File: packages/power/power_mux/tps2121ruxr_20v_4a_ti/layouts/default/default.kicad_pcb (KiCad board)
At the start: 2 copper layers, 13 parts

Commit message: Make package schematics more readable and align passive choices with repo guidance
This pass improves the human-facing quality of the package library.
Explicit local capacitor/resistor parts now carry short descriptive
comments at the point of use, the MCP2518FD package swaps its 1uF bulk
capacitor to a 0603 part to match the current sizing rule, and several
packages add better net-name overrides for exposed and important internal
signals.

Constraint: Repo guidance now prefers explicit local parts and expects readable schematic net names
Constraint: Passive sizing should follow the current MLCC package rule unless a justified exception is needed
Rejected: Keep part instances comment-free | explicit local part names are not readable enough by themselves
Rejected: Leave the MCP2518FD 1uF bulk cap in 0402 | conflicts with the current 1uF-10uF 0603 guidance
Confidence: medium
Scope-risk: moderate
Reversibility: clean
Directive: When instantiating explicit local resistor/capacitor parts, include a short readable comment with the key value/package characteristics unless the name is already obviously human-readable
Tested:  passed for stm32g0b1kbu6_st, mcp2518fdt_e_sl_microchip, tcan3413ddfr_ti, raspberry_pi_hat_socket_zhouri, bq40z50rsmr_r2_4s_3a_ti, tps56637rpar_5v1_5a_ti, tps62933drlr_3v3_ti, bq25756rrvr_4s_2a_ti, tps2121ruxr_20v_4a_ti, and tps25730drefr_20v_3a_ti
Not-tested: Complete elimination of all internal autogenerated net labels in every package; some deep internal nets may still remain tool-driven
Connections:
- net 1 renamed FALLBACK_SEL
- net 1-1 renamed PRIORITY_SEL
- net high_priority-hv renamed HIGH_PRIORITY
- net hv renamed LOW_PRIORITY
- net lv renamed GND
- net out-hv renamed OUT
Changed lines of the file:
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@@
 		)
 	)
-	(net 1 "lv")
-	(net 2 "1")
-	(net 3 "high_priority-hv")
-	(net 4 "out-hv")
+	(net 1 "GND")
+	(net 2 "FALLBACK_SEL")
+	(net 3 "HIGH_PRIORITY")
+	(net 4 "OUT")
 	(net 5 "ILM")
 	(net 6 "SS")
-	(net 7 "hv")
-	(net 8 "1-1")
+	(net 7 "LOW_PRIORITY")
+	(net 8 "PRIORITY_SEL")
 	(net 9 "ST")
 	(footprint "Texas_Instruments_TPS2121RUXR:TPS2121RUXR"
@@
 			(size 0.4 1.05)
 			(layers "F.Cu" "F.Paste" "F.Mask")
-			(net 4 "out-hv")
+			(net 4 "OUT")
 		)
 		(pad "2" smd rect
@@
 			(size 0.4 1.05)
 			(layers "F.Cu" "F.Paste" "F.Mask")
-			(net 7 "hv")
+			(net 7 "LOW_PRIORITY")
 		)
 		(pad "3" smd rect
@@
 			(size 0.2 0.6)
 			(layers "F.Cu" "F.Paste" "F.Mask")
-			(net 2 "1")
+			(net 2 "FALLBACK_SEL")
 		)
 		(pad "4" smd rect
@@
 			(size 0.2 0.6)
 			(layers "F.Cu" "F.Paste" "F.Mask")
-			(net 1 "lv")
+			(net 1 "GND")
 		)
 		(pad "5" smd rect
@@
 			(size 0.2 0.6)
 			(layers "F.Cu" "F.Paste" "F.Mask")
-			(net 1 "lv")
+			(net 1 "GND")
 		)
 		(pad "6" smd rect
@@
 			(size 0.2 0.6)
 			(layers "F.Cu" "F.Paste" "F.Mask")
-			(net 8 "1-1")
+			(net 8 "PRIORITY_SEL")
 		)
 		(pad "7" smd rect
@@
 			(size 0.4 1.05)
 			(layers "F.Cu" "F.Paste" "F.Mask")
-			(net 3 "high_priority-hv")
+			(net 3 "HIGH_PRIORITY")
 		)
 		(pad "8" smd rect
@@
 			(size 0.4 1.05)
 			(layers "F.Cu" "F.Paste" "F.Mask")
-			(net 4 "out-hv")
+			(net 4 "OUT")
 		)
 		(pad "9" smd rect
@@
 			(size 0.2 0.6)
 			(layers "F.Cu" "F.Paste" "F.Mask")
-			(net 1 "lv")
+			(net 1 "GND")
 		)
 	)
@@
 			(size 1.49 1.73)
 			(layers "F.Cu" "F.Paste" "F.Mask")
-			(net 1 "lv")
+			(net 1 "GND")
 		)
 		(pad "1" smd rect
@@
 			(size 1.49 1.73)
 			(layers "F.Cu" "F.Paste" "F.Mask")
-			(net 3 "high_priority-hv")
+			(net 3 "HIGH_PRIORITY")
 		)
 		(embedded_fonts no)
@@
 			(size 0.5 0.54)
 			(layers "F.Cu" "F.Paste" "F.Mask")
-			(net 1 "lv")
+			(net 1 "GND")
 		)
 		(pad "1" smd rect
@@
 			(size 0.5 0.54)
 			(layers "F.Cu" "F.Paste" "F.Mask")
-			(net 3 "high_priority-hv")
+			(net 3 "HIGH_PRIORITY")
 		)
 		(embedded_fonts no)
@@
 			(size 1.49 1.73)
 			(layers "F.Cu" "F.Paste" "F.Mask")
-			(net 1 "lv")
+			(net 1 "GND")
 		)
 		(pad "1" smd rect
@@
 			(size 1.49 1.73)
 			(layers "F.Cu" "F.Paste" "F.Mask")
-			(net 7 "hv")
+			(net 7 "LOW_PRIORITY")
 		)
 		(embedded_fonts no)
@@
 			(size 0.5 0.54)
 			(layers "F.Cu" "F.Paste" "F.Mask")
-			(net 1 "lv")
+			(net 1 "GND")
 		)
 		(pad "1" smd rect
@@
 			(size 0.5 0.54)
 			(layers "F.Cu" "F.Paste" "F.Mask")
-			(net 7 "hv")
+			(net 7 "LOW_PRIORITY")
 		)
 		(embedded_fonts no)
@@
 			(size 1.49 1.73)
 			(layers "F.Cu" "F.Paste" "F.Mask")
-			(net 1 "lv")
+			(net 1 "GND")
 		)
 		(pad "1" smd rect
@@
 			(size 1.49 1.73)
 			(layers "F.Cu" "F.Paste" "F.Mask")
-			(net 4 "out-hv")
+			(net 4 "OUT")
 		)
 		(embedded_fonts no)
@@
 			(size 0.5 0.54)
 			(layers "F.Cu" "F.Paste" "F.Mask")
-			(net 1 "lv")
+			(net 1 "GND")
 		)
 		(pad "1" smd rect
@@
 			(size 0.5 0.54)
 			(layers "F.Cu" "F.Paste" "F.Mask")
-			(net 4 "out-hv")
+			(net 4 "OUT")
 		)
 		(embedded_fonts no)
@@
 			(size 0.57 0.54)
 			(layers "F.Cu" "F.Paste" "F.Mask")
-			(net 8 "1-1")
+			(net 8 "PRIORITY_SEL")
 		)
 		(pad "1" smd rect
@@
 			(size 0.57 0.54)
 			(layers "F.Cu" "F.Paste" "F.Mask")
-			(net 3 "high_priority-hv")
+			(net 3 "HIGH_PRIORITY")
 		)
 		(embedded_fonts no)
@@
 			(size 0.57 0.54)
 			(layers "F.Cu" "F.Paste" "F.Mask")
-			(net 1 "lv")
+			(net 1 "GND")
 		)
 		(pad "1" smd rect
@@
 			(size 0.57 0.54)
 			(layers "F.Cu" "F.Paste" "F.Mask")
-			(net 8 "1-1")
+			(net 8 "PRIORITY_SEL")
 		)
 		(embedded_fonts no)
@@
 			(size 0.57 0.54)
 			(layers "F.Cu" "F.Paste" "F.Mask")
-			(net 2 "1")
+			(net 2 "FALLBACK_SEL")
 		)
 		(pad "1" smd rect
@@
 			(size 0.57 0.54)
 			(layers "F.Cu" "F.Paste" "F.Mask")
-			(net 7 "hv")
+			(net 7 "LOW_PRIORITY")
 		)
 		(embedded_fonts no)
@@
 			(size 0.57 0.54)
 			(layers "F.Cu" "F.Paste" "F.Mask")
-			(net 1 "lv")
+			(net 1 "GND")
 		)
 		(pad "1" smd rect
@@
 			(size 0.57 0.54)
 			(layers "F.Cu" "F.Paste" "F.Mask")
-			(net 2 "1")
+			(net 2 "FALLBACK_SEL")
 		)
 		(embedded_fonts no)
@@
 			(size 0.57 0.54)
 			(layers "F.Cu" "F.Paste" "F.Mask")
-			(net 1 "lv")
+			(net 1 "GND")
 		)
 		(pad "1" smd rect
@@
 			(size 0.5 0.54)
 			(layers "F.Cu" "F.Paste" "F.Mask")
-			(net 1 "lv")
+			(net 1 "GND")
 		)
 		(pad "1" smd rect

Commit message: Finish removing net-name overrides from reusable packages
This completes the package-level override cleanup by deleting the remaining
`override_net_name` assignments from the library's reusable package modules and
rebuilding their checked-in layouts so generated net metadata matches source.
The package interfaces stay the same; only the forced net naming was removed so
these modules compose cleanly when imported into downstream designs.

Constraint: The library must stay reusable and avoid imposed internal net names leaking into consuming designs
Constraint: Each changed package must still verify with the repo's Atopile workflow after layout regeneration
Rejected: Stop after the battery frontend cleanup | leaves the same composition hazard in other packages
Rejected: Remove override lines without rebuilding layouts | would leave stale generated PCB net names checked into the repo
Confidence: high
Scope-risk: moderate
Reversibility: clean
Directive: Do not reintroduce `override_net_name` in reusable package modules unless a package is intentionally design-specific
Tested: `uv tool run --from atopile==0.15.4 ato --non-interactive build` in each affected package directory (stm32g0b1kbu6_st, mcp2518fdt_e_sl_microchip, tcan3413ddfr_ti, raspberry_pi_hat_socket_zhouri, tps56637rpar_5v1_5a_ti, tps62933drlr_3v3_ti, bq25756rrvr_4s_2a_ti, tps2121ruxr_20v_4a_ti, tps25730drefr_20v_3a_ti)
Not-tested: Downstream consumer projects that may have been depending on the old forced net names in generated layouts
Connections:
- net FALLBACK_SEL renamed 1
- net GND renamed lv
- net HIGH_PRIORITY renamed high_priority-hv
- net LOW_PRIORITY renamed hv
- net OUT renamed out-hv
- net PRIORITY_SEL renamed 1-1
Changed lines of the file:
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@@
 		)
 	)
-	(net 1 "GND")
-	(net 2 "FALLBACK_SEL")
-	(net 3 "HIGH_PRIORITY")
-	(net 4 "OUT")
+	(net 1 "lv")
+	(net 2 "1")
+	(net 3 "high_priority-hv")
+	(net 4 "out-hv")
 	(net 5 "ILM")
 	(net 6 "SS")
-	(net 7 "LOW_PRIORITY")
-	(net 8 "PRIORITY_SEL")
+	(net 7 "hv")
+	(net 8 "1-1")
 	(net 9 "ST")
 	(footprint "Texas_Instruments_TPS2121RUXR:TPS2121RUXR"
@@
 			(size 0.4 1.05)
 			(layers "F.Cu" "F.Paste" "F.Mask")
-			(net 4 "OUT")
+			(net 4 "out-hv")
 		)
 		(pad "2" smd rect
@@
 			(size 0.4 1.05)
 			(layers "F.Cu" "F.Paste" "F.Mask")
-			(net 7 "LOW_PRIORITY")
+			(net 7 "hv")
 		)
 		(pad "3" smd rect
@@
 			(size 0.2 0.6)
 			(layers "F.Cu" "F.Paste" "F.Mask")
-			(net 2 "FALLBACK_SEL")
+			(net 2 "1")
 		)
 		(pad "4" smd rect
@@
 			(size 0.2 0.6)
 			(layers "F.Cu" "F.Paste" "F.Mask")
-			(net 1 "GND")
+			(net 1 "lv")
 		)
 		(pad "5" smd rect
@@
 			(size 0.2 0.6)
 			(layers "F.Cu" "F.Paste" "F.Mask")
-			(net 1 "GND")
+			(net 1 "lv")
 		)
 		(pad "6" smd rect
@@
 			(size 0.2 0.6)
 			(layers "F.Cu" "F.Paste" "F.Mask")
-			(net 8 "PRIORITY_SEL")
+			(net 8 "1-1")
 		)
 		(pad "7" smd rect
@@
 			(size 0.4 1.05)
 			(layers "F.Cu" "F.Paste" "F.Mask")
-			(net 3 "HIGH_PRIORITY")
+			(net 3 "high_priority-hv")
 		)
 		(pad "8" smd rect
@@
 			(size 0.4 1.05)
 			(layers "F.Cu" "F.Paste" "F.Mask")
-			(net 4 "OUT")
+			(net 4 "out-hv")
 		)
 		(pad "9" smd rect
@@
 			(size 0.2 0.6)
 			(layers "F.Cu" "F.Paste" "F.Mask")
-			(net 1 "GND")
+			(net 1 "lv")
 		)
 	)
@@
 			(size 1.49 1.73)
 			(layers "F.Cu" "F.Paste" "F.Mask")
-			(net 1 "GND")
+			(net 1 "lv")
 		)
 		(pad "1" smd rect
@@
 			(size 1.49 1.73)
 			(layers "F.Cu" "F.Paste" "F.Mask")
-			(net 3 "HIGH_PRIORITY")
+			(net 3 "high_priority-hv")
 		)
 		(embedded_fonts no)
@@
 			(size 0.5 0.54)
 			(layers "F.Cu" "F.Paste" "F.Mask")
-			(net 1 "GND")
+			(net 1 "lv")
 		)
 		(pad "1" smd rect
@@
 			(size 0.5 0.54)
 			(layers "F.Cu" "F.Paste" "F.Mask")
-			(net 3 "HIGH_PRIORITY")
+			(net 3 "high_priority-hv")
 		)
 		(embedded_fonts no)
@@
 			(size 1.49 1.73)
 			(layers "F.Cu" "F.Paste" "F.Mask")
-			(net 1 "GND")
+			(net 1 "lv")
 		)
 		(pad "1" smd rect
@@
 			(size 1.49 1.73)
 			(layers "F.Cu" "F.Paste" "F.Mask")
-			(net 7 "LOW_PRIORITY")
+			(net 7 "hv")
 		)
 		(embedded_fonts no)
@@
 			(size 0.5 0.54)
 			(layers "F.Cu" "F.Paste" "F.Mask")
-			(net 1 "GND")
+			(net 1 "lv")
 		)
 		(pad "1" smd rect
@@
 			(size 0.5 0.54)
 			(layers "F.Cu" "F.Paste" "F.Mask")
-			(net 7 "LOW_PRIORITY")
+			(net 7 "hv")
 		)
 		(embedded_fonts no)
@@
 			(size 1.49 1.73)
 			(layers "F.Cu" "F.Paste" "F.Mask")
-			(net 1 "GND")
+			(net 1 "lv")
 		)
 		(pad "1" smd rect
@@
 			(size 1.49 1.73)
 			(layers "F.Cu" "F.Paste" "F.Mask")
-			(net 4 "OUT")
+			(net 4 "out-hv")
 		)
 		(embedded_fonts no)
@@
 			(size 0.5 0.54)
 			(layers "F.Cu" "F.Paste" "F.Mask")
-			(net 1 "GND")
+			(net 1 "lv")
 		)
 		(pad "1" smd rect
@@
 			(size 0.5 0.54)
 			(layers "F.Cu" "F.Paste" "F.Mask")
-			(net 4 "OUT")
+			(net 4 "out-hv")
 		)
 		(embedded_fonts no)
@@
 			(size 0.57 0.54)
 			(layers "F.Cu" "F.Paste" "F.Mask")
-			(net 8 "PRIORITY_SEL")
+			(net 8 "1-1")
 		)
 		(pad "1" smd rect
@@
 			(size 0.57 0.54)
 			(layers "F.Cu" "F.Paste" "F.Mask")
-			(net 3 "HIGH_PRIORITY")
+			(net 3 "high_priority-hv")
 		)
 		(embedded_fonts no)
@@
 			(size 0.57 0.54)
 			(layers "F.Cu" "F.Paste" "F.Mask")
-			(net 1 "GND")
+			(net 1 "lv")
 		)
 		(pad "1" smd rect
@@
 			(size 0.57 0.54)
 			(layers "F.Cu" "F.Paste" "F.Mask")
-			(net 8 "PRIORITY_SEL")
+			(net 8 "1-1")
 		)
 		(embedded_fonts no)
@@
 			(size 0.57 0.54)
 			(layers "F.Cu" "F.Paste" "F.Mask")
-			(net 2 "FALLBACK_SEL")
+			(net 2 "1")
 		)
 		(pad "1" smd rect
@@
 			(size 0.57 0.54)
 			(layers "F.Cu" "F.Paste" "F.Mask")
-			(net 7 "LOW_PRIORITY")
+			(net 7 "hv")
 		)
 		(embedded_fonts no)
@@
 			(size 0.57 0.54)
 			(layers "F.Cu" "F.Paste" "F.Mask")
-			(net 1 "GND")
+			(net 1 "lv")
 		)
 		(pad "1" smd rect
@@
 			(size 0.57 0.54)
 			(layers "F.Cu" "F.Paste" "F.Mask")
-			(net 2 "FALLBACK_SEL")
+			(net 2 "1")
 		)
 		(embedded_fonts no)
@@
 			(size 0.57 0.54)
 			(layers "F.Cu" "F.Paste" "F.Mask")
-			(net 1 "GND")
+			(net 1 "lv")
 		)
 		(pad "1" smd rect
@@
 			(size 0.5 0.54)
 			(layers "F.Cu" "F.Paste" "F.Mask")
-			(net 1 "GND")
+			(net 1 "lv")
 		)
 		(pad "1" smd rect

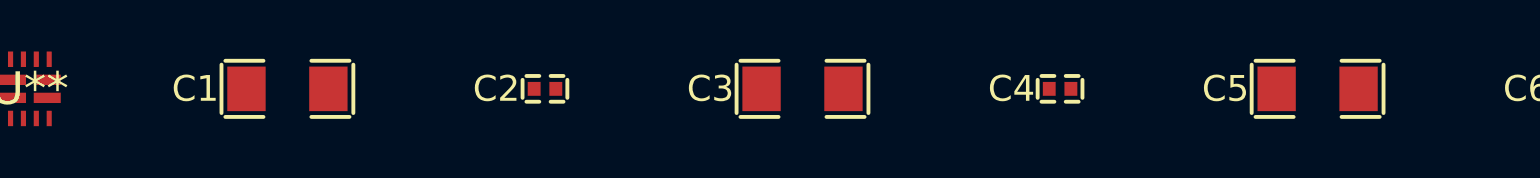
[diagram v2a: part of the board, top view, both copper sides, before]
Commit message: 22uF cap update, TPS56637 update
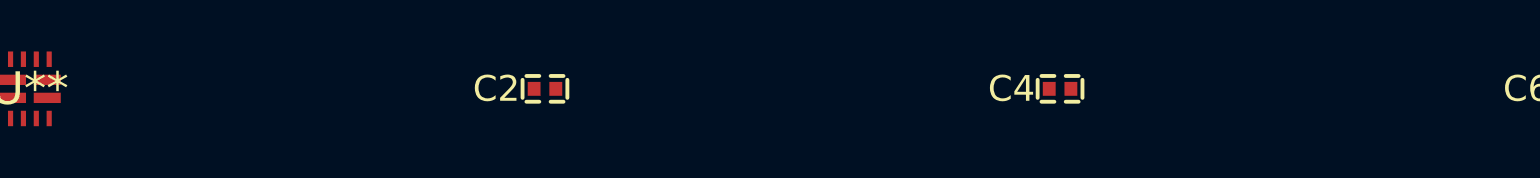
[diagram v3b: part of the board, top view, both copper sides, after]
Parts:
- removed C1, C3, C5: , Murata_Electronics_GRM31CR61H106KA12L:C1206
- C7: footprint Murata_Electronics_GRM155R71H103KA88D:C0402 -> Murata_Electronics_GRM155R71H104KE14D:C0402

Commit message: TPS2121 layout
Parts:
- U**: renamed from U1; value (none) -> TPS2121RUXR
- moved C7 91.5 mm to (37.8, 40.0), turned to 90 degrees
- moved R1 83.6 mm to (37.8, 42.0), turned to -90 degrees
- moved R2 79.7 mm to (31.2, 40.4)
- moved R3 70.6 mm to (31.2, 39.2), turned to 180 degrees
- moved R4 64.1 mm to (31.2, 41.6)
- moved R5 57.7 mm to (31.2, 42.8), turned to 180 degrees
- moved U** 54.1 mm to (35.3, 41.0), turned to -90 degrees
- moved C6 49.2 mm to (37.4, 43.7)
- moved C2 45.4 mm to (31.2, 44.0), turned to 180 degrees
- moved C4 39.0 mm to (31.2, 38.0), turned to 180 degrees
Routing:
- net 1-1: track 0.00 -> 4.72 mm
- net 1: track 0.00 -> 4.71 mm
- net lv: track 0.00 -> 1.75 mm, vias 0 -> 16
- net ILM: track 0.00 -> 1.45 mm
- net SS: track 0.00 -> 1.44 mm
- net out-hv: vias 0 -> 6
- net hv: vias 0 -> 3
- net high_priority-hv: vias 0 -> 3
- added copper zone on B.Cu, net high_priority-hv
- added copper zone on F.Cu, net high_priority-hv
- added copper zone on B.Cu, net hv
- added copper zone on F.Cu, net hv
- added copper zone on B.Cu, net out-hv
- added copper zone on F.Cu, net out-hv
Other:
- copper layers 2 -> 4
